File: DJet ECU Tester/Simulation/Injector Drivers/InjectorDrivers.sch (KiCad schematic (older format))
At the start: 60 parts, among them Q500 BCY58, Q501 BSX95, Q502 AUY21, Q503 AUY21, Q504 BSX95, Q505 BCY58, Q550 BCY58, Q551 BSX95, Q552 AUY21, Q553 AUY21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

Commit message: Updated injector driver simulation to make measuring current consumption easier.
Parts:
- removed V3: 12, symbol Simulation_SPICE:VDC
- added V3, V4, V5: VPULSE, symbol Simulation_SPICE:VPULSE
- added VBOGUS, VINJBOGUS: 0, symbol Simulation_SPICE:VDC
- V2: Spice_Model pulse(0 12 2n 2n 2n 95ms 100ms) -> pulse(0 5 2n 2n 2n 95ms 100ms)
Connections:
- net 0: now also V3.2, V4.2, V5.2, VINJBOGUS.2; no longer R2.1
- net E24-12V: now also VBOGUS.2; no longer V1.1
- net E4-INJ4_8: now also L3.1
- net E5-INJ6_3: now also L2.1
- net E6-INJ7_2: now also L4.1
- net IN_INJ4_8: now also V3.1; no longer R517.2, R567.2
- new net: V1.1, VBOGUS.1
- new net: R2.1, VINJBOGUS.1
- new net IN_INJ6_3: R517.2, V4.1
- new net IN_INJ7_2: R567.2, V5.1
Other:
- note added: ".model DIODE D\n.model BCY58 npn\n.model BSX95 npn\n.model AUY21 pnp\n.tran 1ms 420ms 120m"
- note removed: ".model DIODE D\n.model BCY58 npn\n.model BSX95 npn\n.model AUY21 pnp\n.tran 1ms 300ms 0"
- moved on the sheet: C500, C501, C550, C551, D1, D2, D3, L1, L2, L3, L4, Q500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

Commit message: Increased injectors from four to eight. Added current measurement for injector groups.
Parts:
- added L5, L6, L7, L8: 3.77mH, symbol pspice:INDUCTOR
- added R1, R6, R7, R8: 2.6, Upper Left C wired out to Heat Sink, symbol Device:R_US
- added VINJGROUPBOGUS: 0, symbol Simulation_SPICE:VDC
- renumbered VBOGUS to VBOGUS1, VINJBOGUS to VINJBOGUS1
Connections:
- net 0: now also R2.1, R7.1, R8.1, VINJGROUPBOGUS.2; no longer R3.1
- net E3-INJ1_5: now also L5.1
- net E4-INJ4_8: now also L7.1
- net E5-INJ6_3: now also L6.1
- net E6-INJ7_2: now also L8.1
- net at VINJBOGUS1.1: now also R1.1; no longer R2.1
- new net: L5.2, R1.2
- new net: R3.1, R6.1, VINJGROUPBOGUS.1
- new net: L6.2, R6.2
- new net: L7.2, R7.2
- new net: L8.2, R8.2
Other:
- moved on the sheet: C500, C501, C550, C551, D1, D2, D3, L1, L2, L3, L4, Q500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

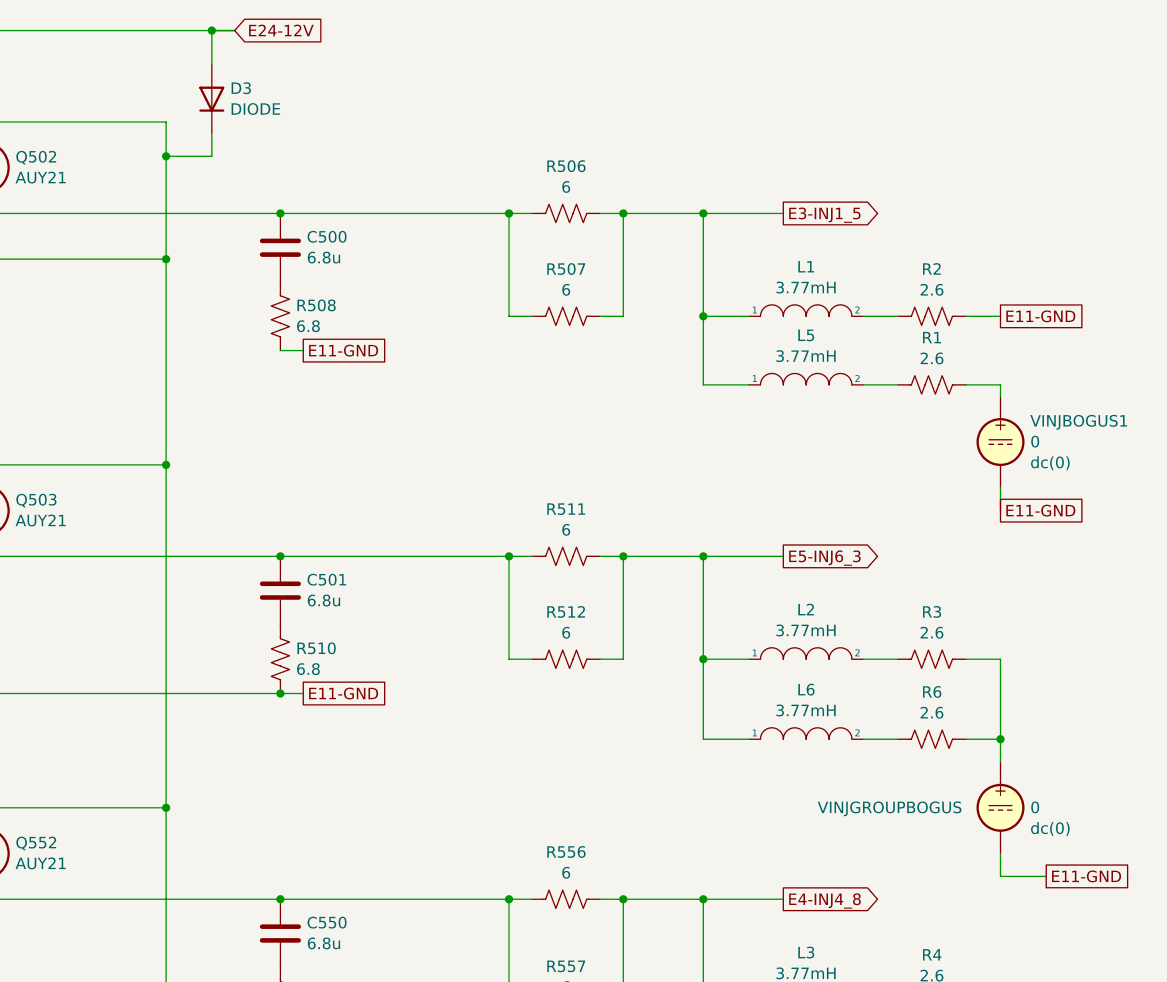
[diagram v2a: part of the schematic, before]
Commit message: Updated temperature support - untested. Switched to Arduino "new" bootloader.
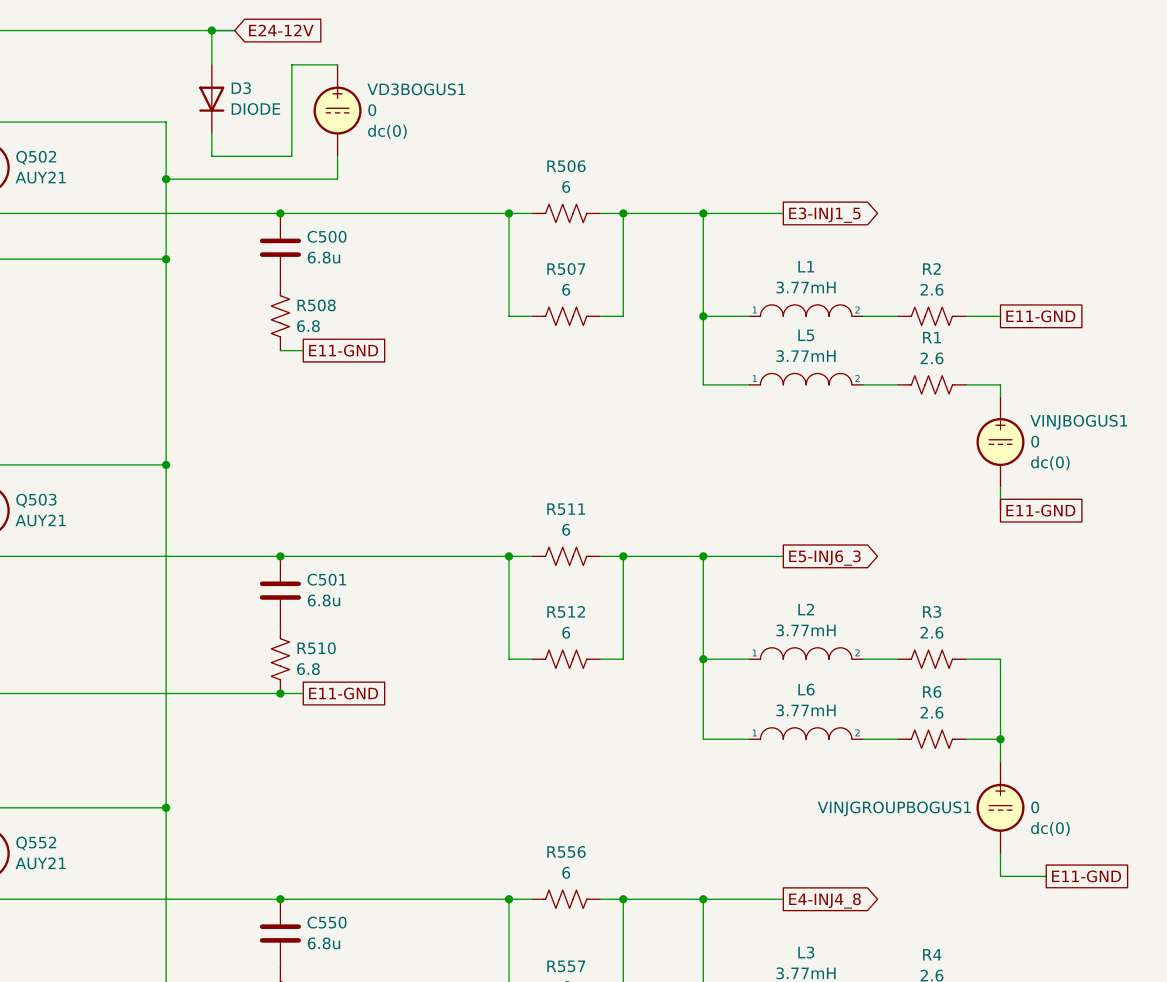
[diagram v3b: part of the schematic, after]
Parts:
- added VD3BOGUS1: 0, symbol Simulation_SPICE:VDC
- renumbered VINJGROUPBOGUS to VINJGROUPBOGUS1
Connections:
- net at Q502.3 (E), Q503.3 (E), Q552.3 (E)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: now also VD3BOGUS1.2; no longer D3.2 (K)
- new net: D3.2 (K), VD3BOGUS1.1
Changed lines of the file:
@@
 	11200 2500 11950 2500
-Wire Wire Line
-	11950 2500 11950 2650
 Wire Wire Line
 	11950 7600 10100 7600
@@
 Wire Wire Line
 	9650 5000 12450 5000
-Wire Wire Line
-	11950 2650 12150 2650
-Connection ~ 11950 2650
-Wire Wire Line
-	11950 2650 11950 3100
 Wire Wire Line
 	10450 2100 12150 2100
@@
 E11-GND
 $Comp
-L Simulation_SPICE:VDC VINJGROUPBOGUS
+L Simulation_SPICE:VDC VINJGROUPBOGUS1
 U 1 1 6057F436
 P 15600 5500
-F 0 "VINJGROUPBOGUS" H 14800 5500 50  0000 L CNN
+F 0 "VINJGROUPBOGUS1" H 14800 5500 50  0000 L CNN
 F 1 "0" H 15730 5500 50  0000 L CNN
 F 2 "" H 15600 5500 50  0001 C CNN
@@
 Wire Wire Line
 	15600 5800 15800 5800
+$Comp
+L Simulation_SPICE:VDC VD3BOGUS1
+U 1 1 606361A5
+P 12700 2450
+F 0 "VD3BOGUS1" H 12830 2541 50  0000 L CNN
+F 1 "0" H 12830 2450 50  0000 L CNN
+F 2 "" H 12700 2450 50  0001 C CNN
+F 3 "~" H 12700 2450 50  0001 C CNN
+F 4 "Y" H 12700 2450 50  0001 L CNN "Spice_Netlist_Enabled"
+F 5 "V" H 12700 2450 50  0001 L CNN "Spice_Primitive"
+F 6 "dc(0)" H 12830 2359 50  0000 L CNN "Spice_Model"
+	1    12700 2450
+	1    0    0    -1
+$EndComp
+Wire Wire Line
+	11950 2500 11950 2750
+Wire Wire Line
+	12150 2650 12500 2650
+Wire Wire Line
+	12500 2650 12500 2250
+Wire Wire Line
+	12500 2250 12700 2250
+Wire Wire Line
+	12700 2650 12700 2750
+Wire Wire Line
+	12700 2750 11950 2750
+Connection ~ 11950 2750
+Wire Wire Line
+	11950 2750 11950 3100
 $EndSCHEMATC

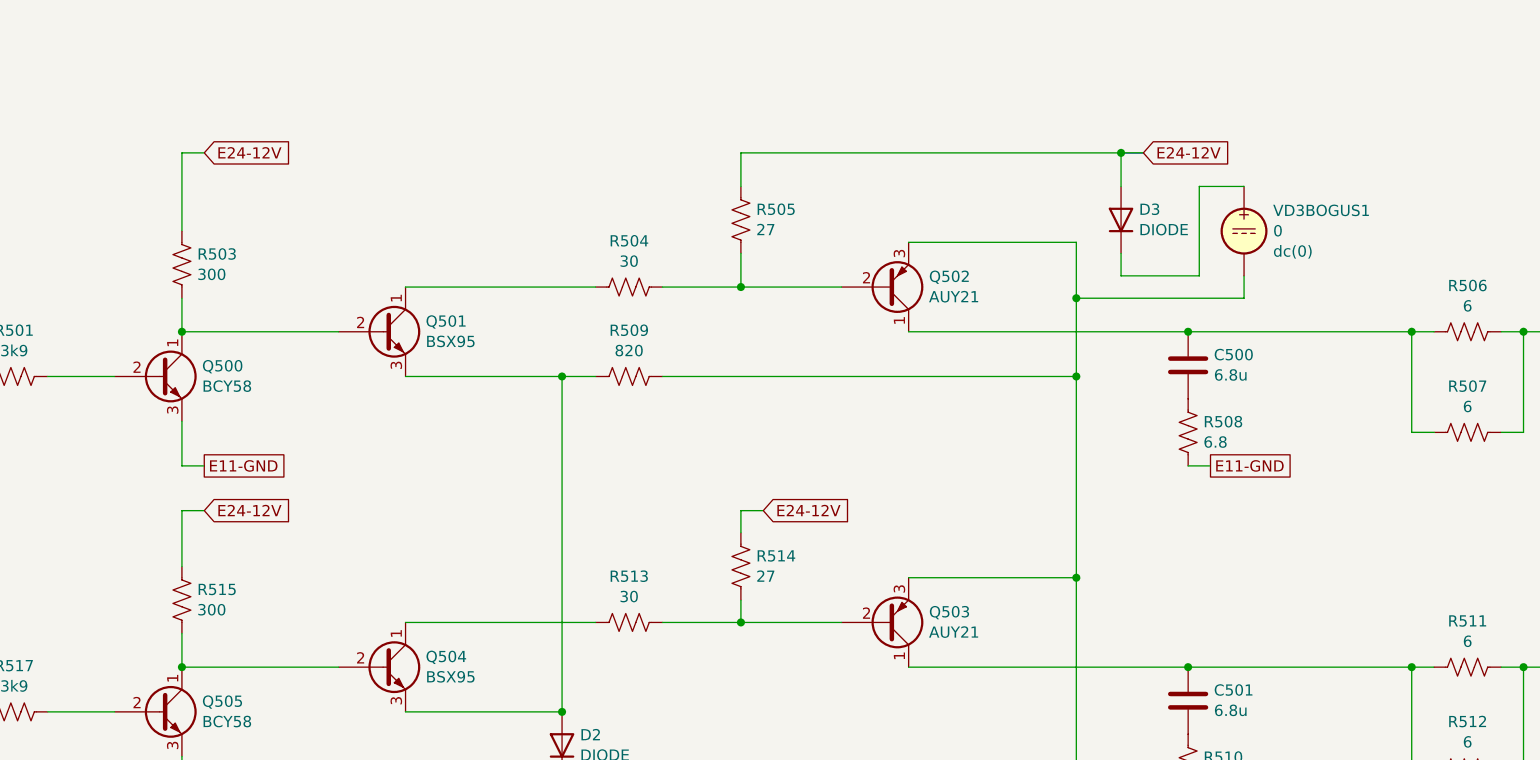
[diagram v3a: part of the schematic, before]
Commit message: Added more current measurements to injector driver simulation.
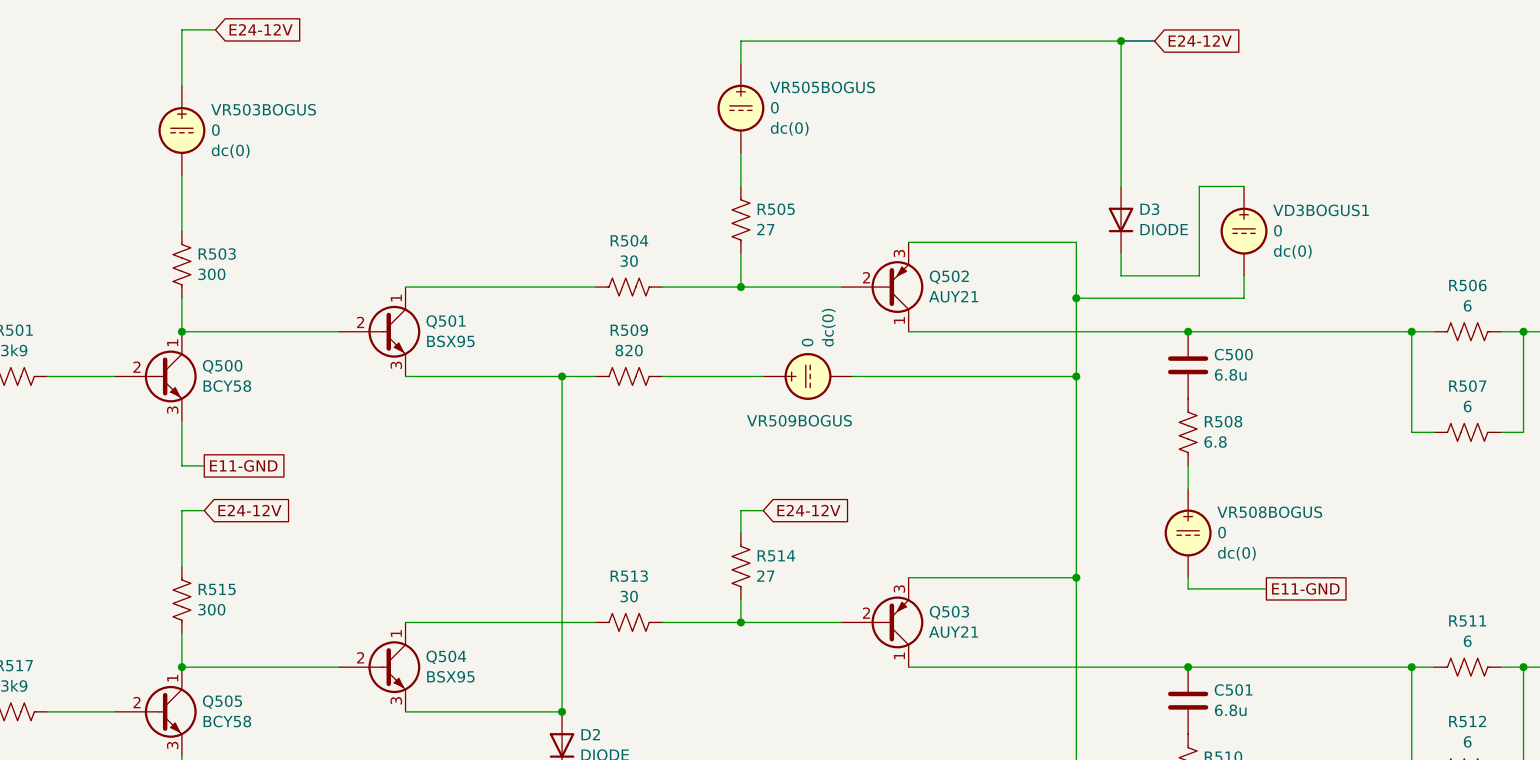
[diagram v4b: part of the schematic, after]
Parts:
- added VR503BOGUS, VR505BOGUS, VR508BOGUS, VR509BOGUS: 0, symbol Simulation_SPICE:VDC
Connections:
- net 0: now also VR508BOGUS.2; no longer R508.2
- net E24-12V: now also VR503BOGUS.1, VR505BOGUS.1; no longer R503.1, R505.1
- net at Q502.3 (E), Q503.3 (E), Q552.3 (E)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: now also VR509BOGUS.2; no longer R509.1
- new net: R508.2, VR508BOGUS.1
- new net: R503.1, VR503BOGUS.2
- new net: R509.1, VR509BOGUS.1
- new net: R505.1, VR505BOGUS.2
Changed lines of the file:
@@
 	1    0    0    -1
 $EndComp
-Text GLabel 8050 2100 2    50   Input ~ 0
+Text GLabel 8100 1550 2    50   Input ~ 0
 E24-12V
 $Comp
@@
 	7950 6300 7950 6500
 Wire Wire Line
-	7950 2450 7950 2100
-Wire Wire Line
 	7950 7800 7950 8000
 Wire Wire Line
@@
 Wire Wire Line
 	9450 7600 9800 7600
-Text GLabel 12250 2100 2    50   Input ~ 0
+Text GLabel 12300 1600 2    50   Input ~ 0
 E24-12V
 Wire Wire Line
@@
 	1    0    0    -1
 $EndComp
-Text GLabel 12550 3500 2    50   UnSpc ~ 0
+Text GLabel 12800 4050 2    50   UnSpc ~ 0
 E11-GND
 Wire Wire Line
@@
 Text GLabel 8050 5000 2    50   UnSpc ~ 0
 E11-GND
-Wire Wire Line
-	10100 3100 11950 3100
-Connection ~ 11950 3100
-Wire Wire Line
-	11950 3100 11950 4000
 $Comp
 L Device:R_US R506
@@
 $EndComp
 Wire Wire Line
-	10450 2250 10450 2100
-Wire Wire Line
 	10450 3800 10450 3700
 Wire Wire Line
@@
 	7950 5000 8050 5000
 Wire Wire Line
-	7950 2100 8050 2100
+	7950 1550 8100 1550
 Wire Wire Line
 	7950 5200 8050 5200
 Wire Wire Line
 	7950 8000 8050 8000
-Wire Wire Line
-	12450 3500 12550 3500
 Wire Wire Line
 	12450 6500 12550 6500
@@
 	9650 5000 12450 5000
 Wire Wire Line
-	10450 2100 12150 2100
-Wire Wire Line
-	12150 2100 12150 2250
-Connection ~ 12150 2100
-Wire Wire Line
-	12150 2100 12250 2100
+	10450 1600 12150 1600
+Wire Wire Line
+	12150 1600 12150 2250
+Connection ~ 12150 1600
+Wire Wire Line
+	12150 1600 12300 1600
 Wire Bus Line
-	12150 2100 12250 2100
+	12150 1600 12300 1600
 Wire Wire Line
 	9100 7600 9100 7650
@@
 	12700 2750 11950 2750
 Connection ~ 11950 2750
+$Comp
+L Simulation_SPICE:VDC VR508BOGUS
+U 1 1 610C9752
+P 12450 3800
+F 0 "VR508BOGUS" H 12580 3891 50  0000 L CNN
+F 1 "0" H 12580 3800 50  0000 L CNN
+F 2 "" H 12450 3800 50  0001 C CNN
+F 3 "~" H 12450 3800 50  0001 C CNN
+F 4 "Y" H 12450 3800 50  0001 L CNN "Spice_Netlist_Enabled"
+F 5 "V" H 12450 3800 50  0001 L CNN "Spice_Primitive"
+F 6 "dc(0)" H 12580 3709 50  0000 L CNN "Spice_Model"
+	1    12450 3800
+	1    0    0    -1
+$EndComp
+Wire Wire Line
+	12450 3500 12450 3600
+Wire Wire Line
+	12450 4000 12450 4050
+Wire Wire Line
+	12450 4050 12800 4050
+$Comp
+L Simulation_SPICE:VDC VR505BOGUS
+U 1 1 611A5D53
+P 10450 1900
+F 0 "VR505BOGUS" H 10580 1991 50  0000 L CNN
+F 1 "0" H 10580 1900 50  0000 L CNN
+F 2 "" H 10450 1900 50  0001 C CNN
+F 3 "~" H 10450 1900 50  0001 C CNN
+F 4 "Y" H 10450 1900 50  0001 L CNN "Spice_Netlist_Enabled"
+F 5 "V" H 10450 1900 50  0001 L CNN "Spice_Primitive"
+F 6 "dc(0)" H 10580 1809 50  0000 L CNN "Spice_Model"
+	1    10450 1900
+	1    0    0    -1
+$EndComp
+Wire Wire Line
+	10450 1700 10450 1600
+Wire Wire Line
+	10450 2100 10450 2250
 Wire Wire Line
 	11950 2750 11950 3100
+Connection ~ 11950 3100
+Wire Wire Line
+	11950 3100 11950 4000
+$Comp
+L Simulation_SPICE:VDC VR509BOGUS
+U 1 1 611C586E
+P 10750 3100
+F 0 "VR509BOGUS" V 10550 2900 50  0000 L CNN
+F 1 "0" H 10880 3100 50  0000 L CNN
+F 2 "" H 10750 3100 50  0001 C CNN
+F 3 "~" H 10750 3100 50  0001 C CNN
+F 4 "Y" H 10750 3100 50  0001 L CNN "Spice_Netlist_Enabled"
+F 5 "V" H 10750 3100 50  0001 L CNN "Spice_Primitive"
+F 6 "dc(0)" H 10880 3009 50  0000 L CNN "Spice_Model"
+	1    10750 3100
+	0    -1   -1   0
+$EndComp
+Wire Wire Line
+	10950 3100 11950 3100
+Wire Wire Line
+	10550 3100 10100 3100
+$Comp
+L Simulation_SPICE:VDC VR503BOGUS
+U 1 1 611EF31B
+P 7950 2000
+F 0 "VR503BOGUS" H 8080 2091 50  0000 L CNN
+F 1 "0" H 8080 2000 50  0000 L CNN
+F 2 "" H 7950 2000 50  0001 C CNN
+F 3 "~" H 7950 2000 50  0001 C CNN
+F 4 "Y" H 7950 2000 50  0001 L CNN "Spice_Netlist_Enabled"
+F 5 "V" H 7950 2000 50  0001 L CNN "Spice_Primitive"
+F 6 "dc(0)" H 8080 1909 50  0000 L CNN "Spice_Model"
+	1    7950 2000
+	1    0    0    -1
+$EndComp
+Wire Wire Line
+	7950 1550 7950 1800
+Wire Wire Line
+	7950 2200 7950 2450
 $EndSCHEMATC
